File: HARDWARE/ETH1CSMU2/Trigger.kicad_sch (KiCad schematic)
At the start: 22 parts, among them U701 TXB0104PW, U702 ADuM5402, U703 74AC125

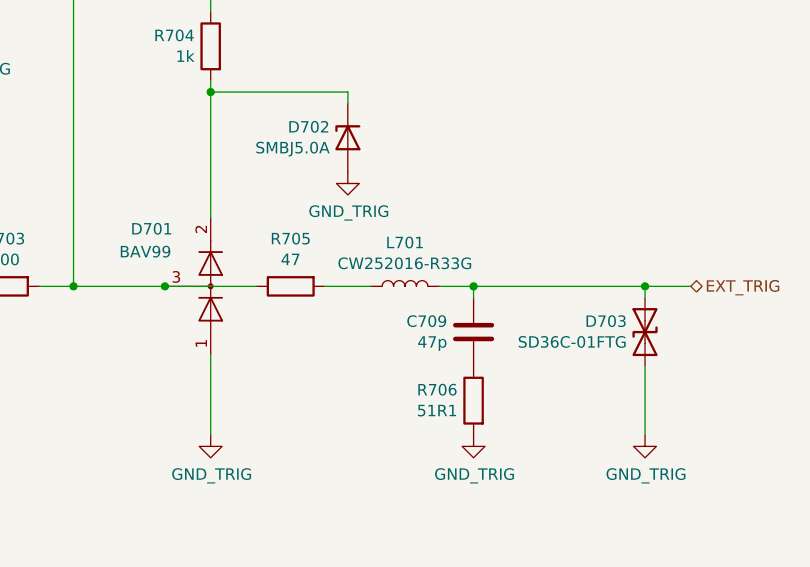
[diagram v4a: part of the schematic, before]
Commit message: Converter HW to KiCAD 7.0. Fixed 3D model paths.
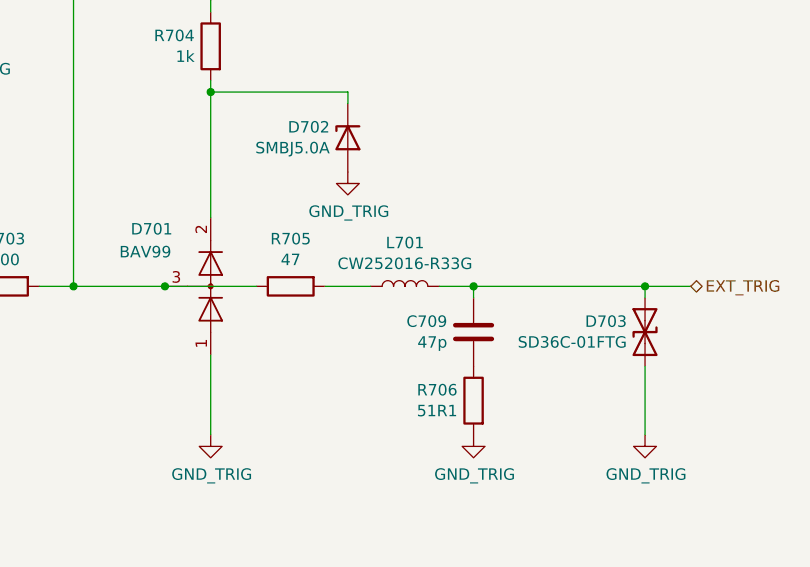
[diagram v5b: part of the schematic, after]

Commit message: Development
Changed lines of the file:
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@@
   )
   (polyline (pts (xy 115.57 99.06) (xy 115.57 191.77))
-    (stroke (width 0) (type default))
+    (stroke (width 0) (type dash))
   )
   (wire (pts (xy 137.16 115.57) (xy 138.43 115.57))
@@
   )
   (polyline (pts (xy 115.57 15.24) (xy 115.57 69.85))
-    (stroke (width 0) (type default))
+    (stroke (width 0) (type dash))
   )
   (wire (pts (xy 102.87 78.74) (xy 90.17 78.74))
